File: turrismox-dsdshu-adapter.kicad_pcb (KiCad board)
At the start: 2 copper layers, 112 x 25 mm, 2 parts, among them J1 Conn_01x06, J2 Conn_02x17_Odd_Even

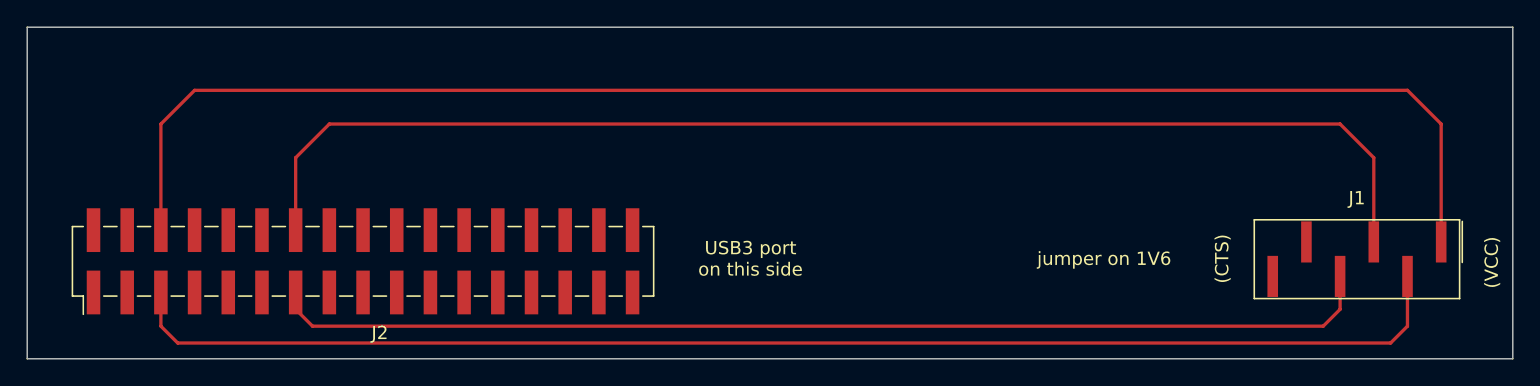
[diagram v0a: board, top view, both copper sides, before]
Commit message: set plotting settings, add mounting hole footprint
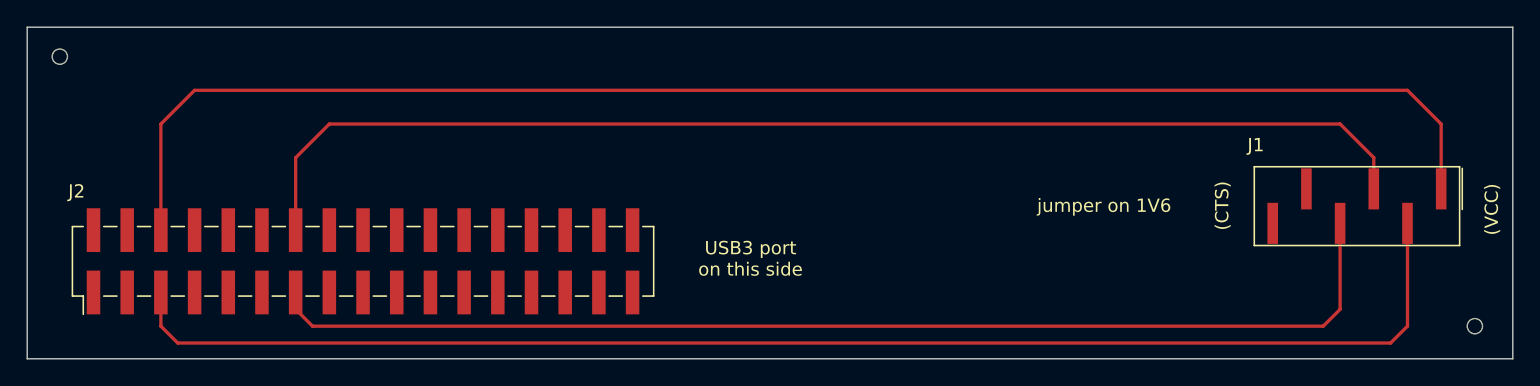
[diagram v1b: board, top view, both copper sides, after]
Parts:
- added REF**: JLCPCB_Mounting_Hole, footprints:JLCPCB_Mounting_Hole, F.Cu at (73.7, 83.8)
- added REF**: JLCPCB_Mounting_Hole, footprints:JLCPCB_Mounting_Hole, F.Cu at (180.3, 104.1)
- moved J1 4.00 mm to (177.8, 93.8)
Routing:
- net /VCC: track 115.5 -> 111.5 mm
- net /MoxT: track 83.5 -> 87.5 mm
- net /GND: track 101.3 -> 105.3 mm
- net /MoxR: track 95.2 -> 91.2 mm

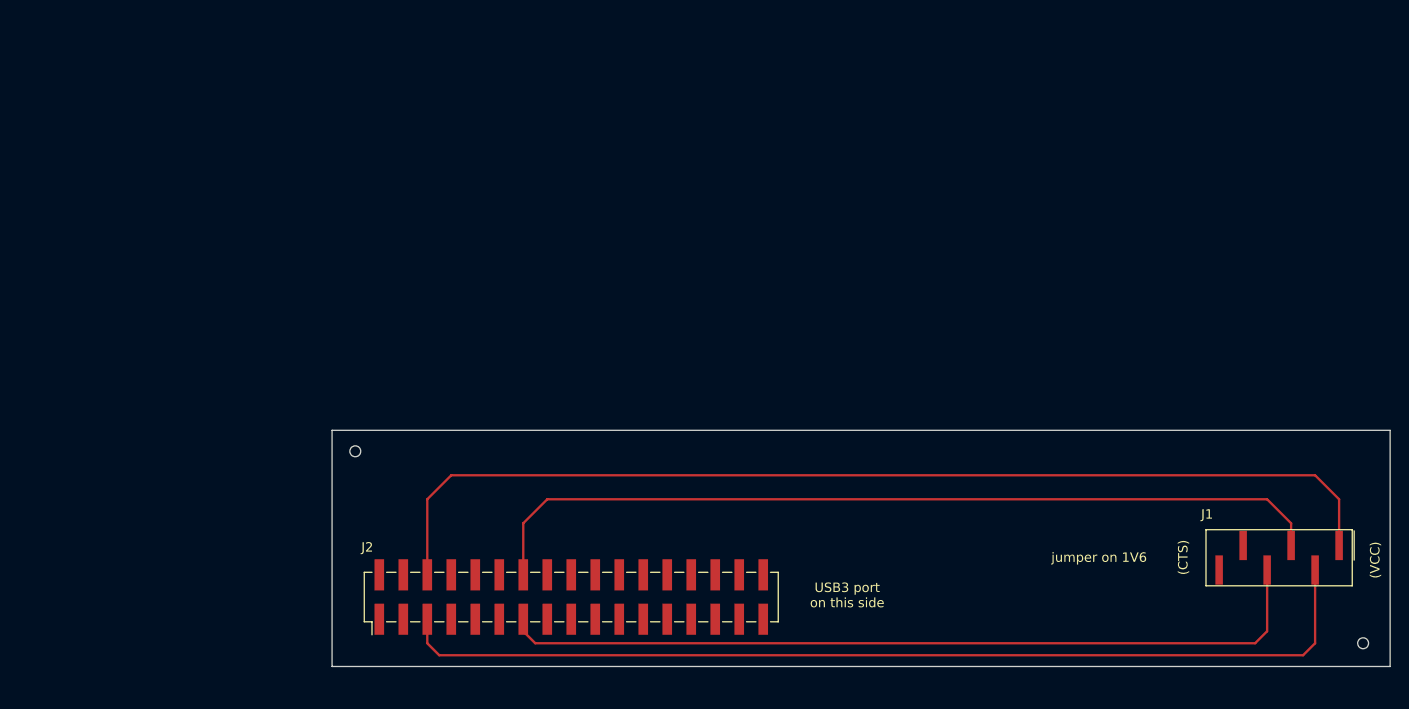
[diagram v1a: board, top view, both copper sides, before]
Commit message: change design to use ribbon cable for Mox connection
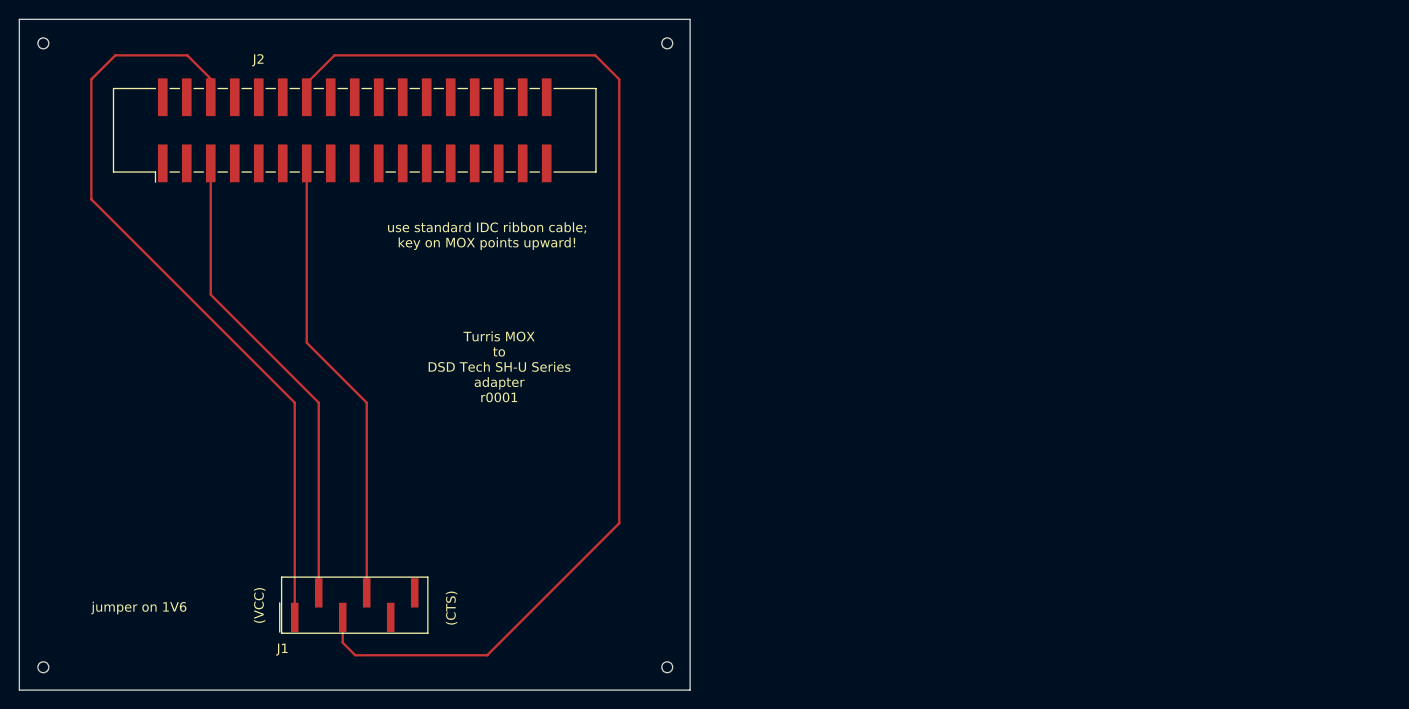
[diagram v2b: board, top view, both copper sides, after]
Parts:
- removed the REF** at (73.7, 83.8)
- removed the REF** at (180.3, 104.1)
- added REF**: JLCPCB_Mounting_Hole, footprints:JLCPCB_Mounting_Hole, F.Cu at (106.7, 40.6)
- added REF**: JLCPCB_Mounting_Hole, footprints:JLCPCB_Mounting_Hole, F.Cu at (106.7, 106.7)
- added REF**: JLCPCB_Mounting_Hole, footprints:JLCPCB_Mounting_Hole, F.Cu at (40.6, 40.6)
- added REF**: JLCPCB_Mounting_Hole, footprints:JLCPCB_Mounting_Hole, F.Cu at (40.6, 106.7)
- J2: footprint footprints:Liansheng FH-00357 -> footprints:Ckmtw_B-3000N34P-0110
- moved J1 110.8 mm to (67.2, 101.4), turned to 0 degrees
- moved J2 53.4 mm to (53.3, 53.3)
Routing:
- net /GND: track 105.3 -> 50.2 mm
- net /MoxT: track 87.5 -> 48.1 mm
- net /MoxR: track 91.2 -> 122.1 mm
- net /VCC: track 111.5 -> 82.6 mm
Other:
- board size 112 x 25 mm -> 71 x 71 mm
- board text added: "Turris MOX to DSD Tech SH-U Series adapter r0001"
- board text added: "use standard IDC ribbon cable; key on MOX points upward!"
- board text removed: "USB3 port on this side"

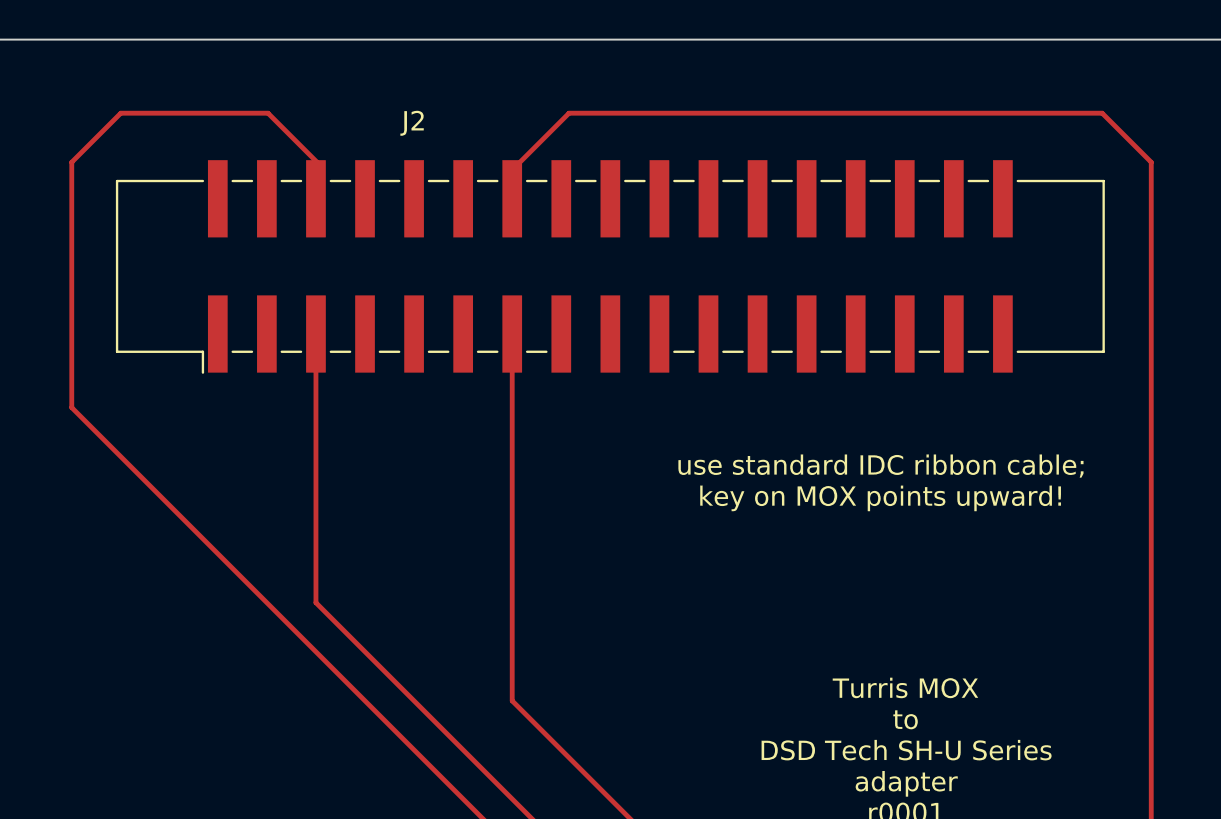
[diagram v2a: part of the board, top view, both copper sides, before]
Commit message: JLCPCB denied my part request; now they have to solder it by hand (THT)
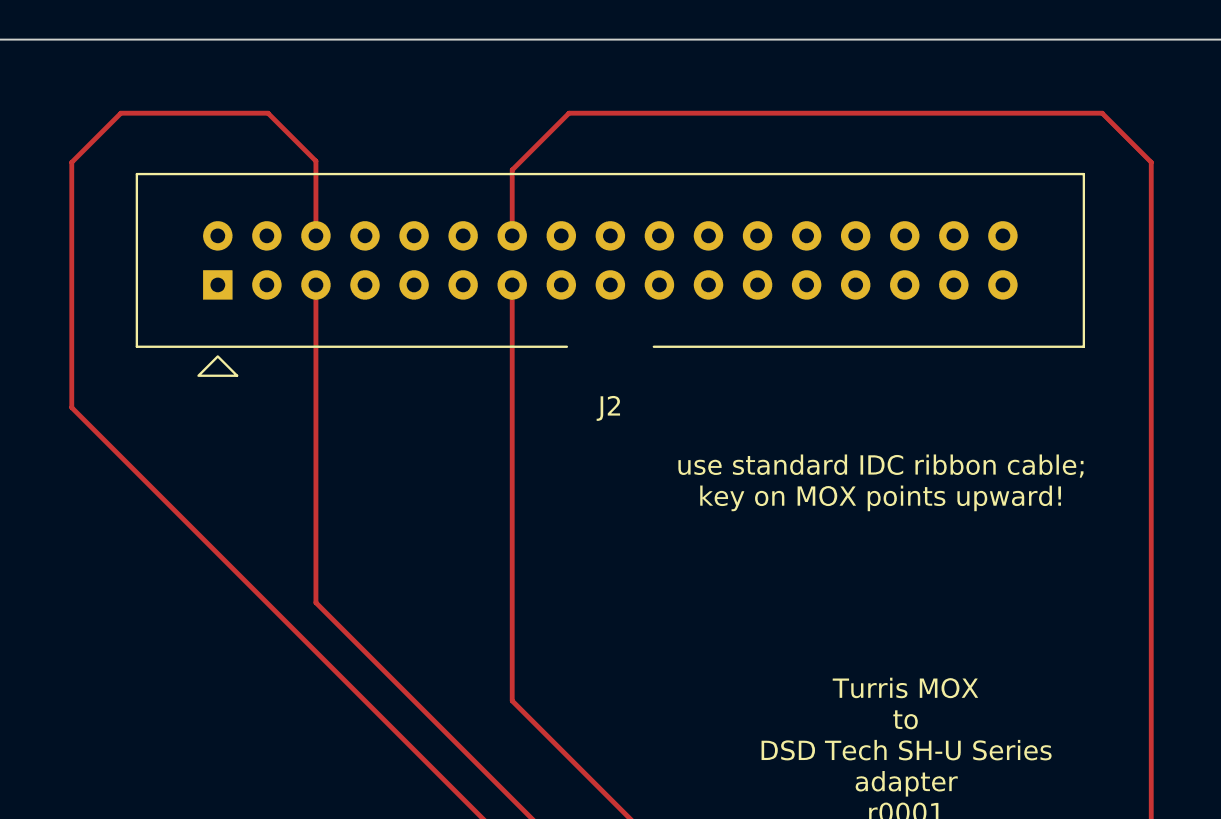
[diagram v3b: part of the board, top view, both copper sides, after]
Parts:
- J2: footprint footprints:Ckmtw_B-3000N34P-0110 -> footprints:JILN_321034SG0ABK00A01
- moved J2 2.54 mm to (53.3, 50.8)
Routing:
- net /MoxT: track 48.1 -> 50.6 mm
- net /GND: track 50.2 -> 52.7 mm
- net /MoxR: track 122.1 -> 124.0 mm
- net /VCC: track 82.6 -> 84.5 mm
